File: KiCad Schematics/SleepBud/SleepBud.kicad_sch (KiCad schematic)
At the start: 134 parts, among them J1 USB_B_Micro, J2 12V, Q1 AO3400A, Q2 FQP27P06, SW1 Mode, SW2 Up Button, SW3 Down Button, SW4 EN Button, SW5 SW_Push, SW6 SW_Push, U1 ESP32-S3-WROOM-1, U2 DS3231SN_, U3 PIR, U4 AMS1117-3.3, U5 AMS1117-5.0, U6 TXS0108EPW

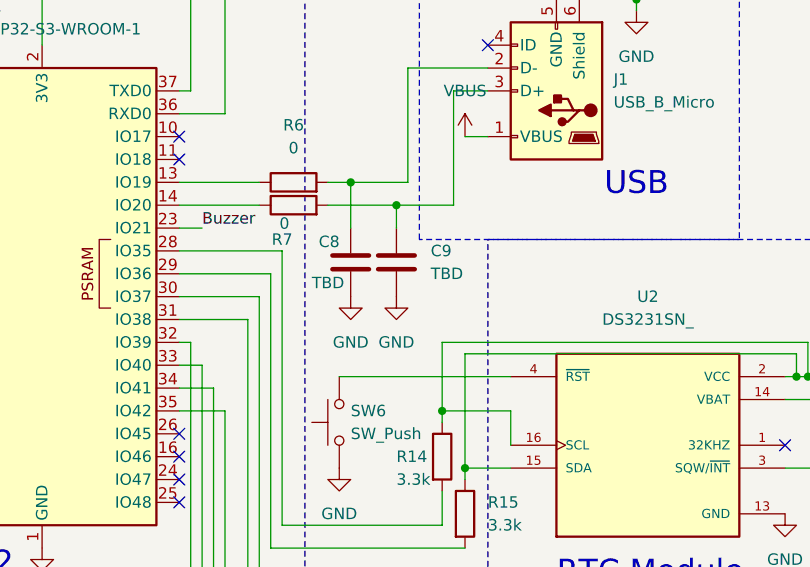
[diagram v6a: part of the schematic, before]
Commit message: Added Footprints to most things
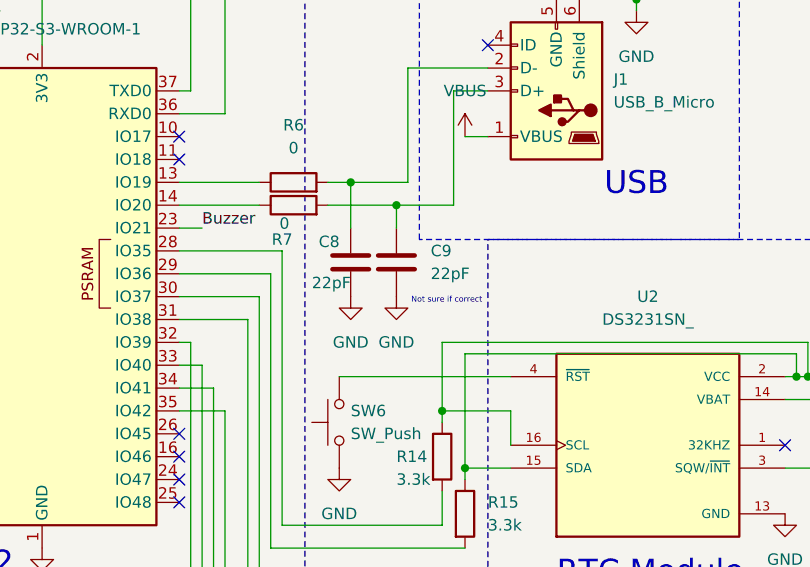
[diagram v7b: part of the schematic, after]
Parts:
- C1, C2, C3, C4, C6: footprint (none) -> Capacitor_SMD:C_0805_2012Metric
- C10, C11, C12, C13, C14, C5, C7: footprint (none) -> Capacitor_SMD:C_0603_1608Metric
- C8, C9: value TBD -> 22pF; footprint (none) -> Capacitor_SMD:C_0603_1608Metric
- R1, R10, R11, R12, R13, R16, R17, R18, R19, R2, R20, R3, R5, R6, R7, R8, R9: footprint (none) -> Resistor_SMD:R_1206_3216Metric
- R14, R15: footprint (none) -> Resistor_SMD:R_0805_2012Metric
- R4: footprint (none) -> Resistor_SMD:R_0201_0603Metric
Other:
- note added: "Not sure if correct"
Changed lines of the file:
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@@
 		)
 	)
+	(text "Not sure if correct"
+		(exclude_from_sim no)
+		(at 211.328 65.278 0)
+		(effects
+			(font
+				(size 0.635 0.635)
+			)
+		)
+	)
 	(text "This is its own PCB with its \nown PINS sticking out."
 		(exclude_from_sim no)
@@
 			)
 		)
-		(property "Footprint" ""
+		(property "Footprint" "Resistor_SMD:R_0805_2012Metric"
 			(at 211.582 88.9 90)
 			(effects
@@
 			)
 		)
-		(property "Footprint" ""
+		(property "Footprint" "Resistor_SMD:R_1206_3216Metric"
 			(at 240.792 119.38 90)
 			(effects
@@
 			)
 		)
-		(property "Footprint" ""
+		(property "Footprint" "Resistor_SMD:R_1206_3216Metric"
 			(at 131.572 54.61 90)
 			(effects
@@
 			)
 		)
-		(property "Value" "TBD"
+		(property "Value" "22pF"
 			(at 209.55 62.2299 0)
 			(effects
@@
 			)
 		)
-		(property "Footprint" ""
+		(property "Footprint" "Capacitor_SMD:C_0603_1608Metric"
 			(at 206.7052 64.77 0)
 			(effects
@@
 			)
 		)
-		(property "Footprint" ""
+		(property "Footprint" "Capacitor_SMD:C_0603_1608Metric"
 			(at 115.2652 25.4 0)
 			(effects
@@
 			)
 		)
-		(property "Footprint" ""
+		(property "Footprint" "Capacitor_SMD:C_0805_2012Metric"
 			(at 42.8752 87.63 0)
 			(effects
@@
 			)
 		)
-		(property "Footprint" ""
+		(property "Footprint" "Capacitor_SMD:C_0805_2012Metric"
 			(at 106.3752 25.4 0)
 			(effects
@@
 			)
 		)
-		(property "Footprint" ""
+		(property "Footprint" "Resistor_SMD:R_1206_3216Metric"
 			(at 123.952 53.34 90)
 			(effects
@@
 			)
 		)
-		(property "Footprint" ""
+		(property "Footprint" "Resistor_SMD:R_1206_3216Metric"
 			(at 143.002 59.69 90)
 			(effects
@@
 			)
 		)
-		(property "Footprint" ""
+		(property "Footprint" "Resistor_SMD:R_1206_3216Metric"
 			(at 21.082 33.02 90)
 			(effects
@@
 			)
 		)
-		(property "Footprint" ""
+		(property "Footprint" "Resistor_SMD:R_0805_2012Metric"
 			(at 209.042 82.55 90)
 			(effects
@@
 			)
 		)
-		(property "Footprint" ""
+		(property "Footprint" "Capacitor_SMD:C_0603_1608Metric"
 			(at 129.54 28.2448 0)
 			(effects
@@
 			)
 		)
-		(property "Footprint" ""
+		(property "Footprint" "Resistor_SMD:R_0201_0603Metric"
 			(at 253.492 77.47 90)
 			(effects
@@
 			)
 		)
-		(property "Footprint" ""
+		(property "Footprint" "Capacitor_SMD:C_0603_1608Metric"
 			(at 265.1252 81.28 0)
 			(effects
@@
 			)
 		)
-		(property "Footprint" ""
+		(property "Footprint" "Capacitor_SMD:C_0603_1608Metric"
 			(at 275.2852 105.41 0)
 			(effects
@@
 			)
 		)
-		(property "Footprint" ""
+		(property "Footprint" "Capacitor_SMD:C_0805_2012Metric"
 			(at 65.7352 87.63 0)
 			(effects
@@
 			)
 		)
-		(property "Footprint" ""
+		(property "Footprint" "Resistor_SMD:R_1206_3216Metric"
 			(at 125.73 23.368 90)
 			(effects
@@
 			)
 		)
-		(property "Footprint" ""
+		(property "Footprint" "Capacitor_SMD:C_0603_1608Metric"
 			(at 319.7352 114.3 0)
 			(effects
@@
 			)
 		)
-		(property "Footprint" ""
+		(property "Footprint" "Resistor_SMD:R_1206_3216Metric"
 			(at 261.62 224.028 90)
 			(effects
@@
 			)
 		)
-		(property "Footprint" ""
+		(property "Footprint" "Resistor_SMD:R_1206_3216Metric"
 			(at 261.62 203.708 90)
 			(effects
@@
 			)
 		)
-		(property "Footprint" ""
+		(property "Footprint" "Capacitor_SMD:C_0805_2012Metric"
 			(at 78.4352 38.1 0)
 			(effects
@@
 			)
 		)
-		(property "Footprint" ""
+		(property "Footprint" "Resistor_SMD:R_1206_3216Metric"
 			(at 113.03 38.608 90)
 			(effects
@@
 			)
 		)
-		(property "Footprint" ""
+		(property "Footprint" "Capacitor_SMD:C_0805_2012Metric"
 			(at 55.5752 38.1 0)
 			(effects
@@
 			)
 		)
-		(property "Footprint" ""
+		(property "Footprint" "Resistor_SMD:R_1206_3216Metric"
 			(at 261.62 183.388 90)
 			(effects
@@
 			)
 		)
-		(property "Footprint" ""
+		(property "Footprint" "Resistor_SMD:R_1206_3216Metric"
 			(at 261.62 244.348 90)
 			(effects
@@
 			)
 		)
-		(property "Footprint" ""
+		(property "Footprint" "Resistor_SMD:R_1206_3216Metric"
 			(at 261.62 161.798 90)
 			(effects
@@
 			)
 		)
-		(property "Footprint" ""
+		(property "Footprint" "Resistor_SMD:R_1206_3216Metric"
 			(at 137.922 57.15 90)
 			(effects
@@
 			)
 		)
-		(property "Footprint" ""
+		(property "Footprint" "Capacitor_SMD:C_0603_1608Metric"
 			(at 284.1752 85.09 0)
 			(effects
@@
 			)
 		)
-		(property "Footprint" ""
+		(property "Footprint" "Capacitor_SMD:C_0603_1608Metric"
 			(at 104.14 43.4848 0)
 			(effects
@@
 			)
 		)
-		(property "Footprint" ""
+		(property "Footprint" "Resistor_SMD:R_1206_3216Metric"
 			(at 194.31 56.388 90)
 			(effects
@@
 			)
 		)
-		(property "Footprint" ""
+		(property "Footprint" "Resistor_SMD:R_1206_3216Metric"
 			(at 22.86 173.228 90)
 			(effects
@@
 			)
 		)
-		(property "Value" "TBD"
+		(property "Value" "22pF"
 			(at 196.342 63.246 0)
 			(effects
@@
 			)
 		)
-		(property "Footprint" ""
+		(property "Footprint" "Capacitor_SMD:C_0603_1608Metric"
 			(at 201.6252 64.77 0)
 			(effects
@@
 			)
 		)
-		(property "Footprint" ""
+		(property "Footprint" "Resistor_SMD:R_1206_3216Metric"
 			(at 194.31 53.848 90)
 			(effects
@@
 			)
 		)
-		(property "Footprint" ""
+		(property "Footprint" "Resistor_SMD:R_1206_3216Metric"
 			(at 350.52 39.878 90)
 			(effects

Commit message: Finish Most Footprint, Started Layout
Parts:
- added U7: Lamp SMD, Connector_PinHeader_1.00mm:PinHeader_1x03_P1.00mm_Vertical_SMD_Pin1Right, symbol LampSignals:Lamp_Power
- BT1: footprint (none) -> Battery:BatteryHolder_Keystone_1057_1x2032
- CR1: footprint SDO_SOD-123FL498_OSI -> footprints:SDO_SOD-123FL498_OSI
- J1: footprint (none) -> Connector_USB:USB_Micro-B_Molex-105017-0001
- J2: value 12V -> 12V Barrel Jack; footprint (none) -> Connector_BarrelJack:BarrelJack_Wuerth_694108106102_2.5x5.5mm
- JP1, JP2: footprint (none) -> Connector_PinHeader_1.00mm:PinHeader_2x02_P1.00mm_Vertical_SMD
- JP3: footprint (none) -> Connector_PinHeader_1.00mm:PinHeader_2x01_P1.00mm_Vertical_SMD
- SW1: value Mode -> Mode Button; footprint (none) -> Button_Switch_SMD:SW_SPST_B3S-1000
- SW2, SW3: footprint (none) -> Button_Switch_SMD:SW_SPST_B3S-1000
- SW4: footprint (none) -> Button_Switch_SMD:SW_Tactile_SPST_NO_Straight_CK_PTS636Sx25SMTRLFS
- SW5: value SW_Push -> Switch Button; footprint (none) -> Button_Switch_SMD:SW_SPST_B3S-1000
- SW6: value SW_Push -> Reset Button; footprint (none) -> Button_Switch_SMD:SW_Tactile_SPST_NO_Straight_CK_PTS636Sx25SMTRLFS
- U3: footprint (none) -> Connector_PinHeader_1.00mm:PinHeader_1x03_P1.00mm_Vertical_SMD_Pin1Left
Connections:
- net +5V: now also U7.1 (VCC)
- net GND: now also U7.3 (GND)
- net at D46.4 (DIN): no longer R2.2
- new net: R2.2, U7.2 (DIN)
- no-connect marks 23 -> 24
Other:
- note added: "prob change mosfet that can be smd"
- moved on the sheet: BZ1, Q1, R16, R2
